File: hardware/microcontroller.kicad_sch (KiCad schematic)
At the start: 53 parts, among them J501 TC2050, J502 PRPC006SAAN-RC, J503 61300611121, J504 61300611121, J505 61300611121, J506 61300611121, J507 61300611121, J508 PRPC001DAAN-RC, J509 PRPC006SAAN-RC, SW501 430182050816, SW502 430182050816, U501 STM32L552CEU6, U502 AT25SF081B-MAHB-T, Y501 ECS-160-9-37-CKM-TR3, Y502 ABS05-32.768KHZ-9-T

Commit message: HW: Refactor the schematics
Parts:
- removed R504: 10 kΩ, perfect_footprints:R_0402_1005Metric, symbol Device:R
- added C516: 0.1 µF, perfect_footprints:C_0402_1005Metric, symbol Device:C
- added Q401: BSS806NH, Package_TO_SOT_SMD:SOT-23-3, symbol Transistor_FET:Q_NMOS_GSD
- added R403: 180 kΩ, perfect_footprints:R_0402_1005Metric, symbol Device:R
- added R404: 330 Ω, perfect_footprints:R_0402_1005Metric, symbol Device:R
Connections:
- net BAT_DETn: now also Q401.1 (G); no longer U501.11 (PA1)
- net EXT_FLASH_NCS: now also R511.2, U502.1 (~{CS}); no longer R511.1, U501.22 (PB11)
- net EXT_FLASH_SCK: now also R512.2, U502.6 (SCK); no longer R512.1, U501.21 (PB10)
- net GND: now also C516.2, Q401.2 (S)
- net V_3V3: now also R403.1
- net I2C_SCL renamed I2C.SCL
- net I2C_SDA renamed I2C.SDA
- net USB_DN renamed USB.DM
- net USB_DP renamed USB.DP
- net VDDA renamed V_DDA
- new net: C516.1, Q401.3 (D), R403.2, R404.1
- new net: R512.1, U501.21 (PB10)
- new net: R511.1, U501.22 (PB11)
- new net BAT_DET: R404.2, U501.11 (PA1)
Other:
- note removed: "Debug header"
- note removed: "Place R506 near the MCU pin. Place R502 near the connector."
- note removed: "Place the capacitor near the MCU pin."
- note removed: "Reset switch"
- note removed: "Use a common center pad."
- moved on the sheet: R503, R505, R511, R512

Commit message: Add EEPROM
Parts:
- removed C514, C516: 0.1 µF, perfect_footprints:C_0402_1005Metric, symbol Device:C
- removed R502, R506, R507, R511, R512, R513, R514, R515, R516: 22 Ω, perfect_footprints:R_0402_1005Metric, symbol Device:R
- removed R517, R518, R519, R520: 10 kΩ, perfect_footprints:R_0402_1005Metric, symbol Device:R
- removed U502: AT25SF081B-MAHB-T, Package_DFN_QFN:DFN-8-1EP_2x3mm_P0.5mm_EP0.61x2.2mm, symbol Renesas:AT25SF081-MAHB-X
- added C222: 1 µF, perfect_footprints:C_0201_0603Metric, symbol Device:C
- added R523, R524, R525, R526, R527: 27 Ω, perfect_footprints:R_0201_0603Metric, symbol Device:R
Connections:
- net DBG_UART_RX: now also J502.4 (Pin_4), R527.1; no longer U501.13 (PA3)
- net DBG_UART_TX: now also R526.2
- net GND: now also C222.2
- net MDM_TXD: now also R525.2
- net at J502.5 (Pin_5): now also R526.1
- net at Q401.3 (D), R403.2, R404.1: now also C222.1
- net at U501.42 (PB6): now also R525.1
- net at U501.21 (PB10): now also R524.1
- net at U501.22 (PB11): now also R523.1
- net EXT_FLASH_IO0 renamed FLASH_QSPI.IO0
- net EXT_FLASH_IO1 renamed FLASH_QSPI.IO1
- net EXT_FLASH_IO2 renamed FLASH_QSPI.IO2
- net EXT_FLASH_IO3 renamed FLASH_QSPI.IO3
- net HWID_1: no longer names the net of U501.14 (PA4)
- net HWID_2: no longer names the net of U501.15 (PA5)
- new net: R527.2, U501.13 (PA3)
- new net FLASH_QSPI.CSn: R523.2
- new net FLASH_QSPI.SCK: R524.2
- no-connect marks 9 -> 11
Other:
- note removed: "External flash"
- note removed: "Hardware ID map"
- note removed: "Use common center pads."
- moved on the sheet: R509

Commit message: Refine schematics
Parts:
- removed C501, C503, C504, C507, C508, C512, C515: 0.1 µF, perfect_footprints:C_0402_1005Metric, symbol Device:C
- removed C502, C513: 4.7 µF, Capacitor_SMD:C_0603_1608Metric, symbol Device:C
- removed C509: 0.01 μF, perfect_footprints:C_0402_1005Metric, symbol Device:C
- removed R403: 180 kΩ, perfect_footprints:R_0402_1005Metric, symbol Device:R
- removed R404, R503, R521: 330 Ω, perfect_footprints:R_0402_1005Metric, symbol Device:R
- removed R501, R505, R522: 10 kΩ, perfect_footprints:R_0402_1005Metric, symbol Device:R
- removed R508, R509: 4.7 kΩ, perfect_footprints:R_0402_1005Metric, symbol Device:R
- removed R510: 0 Ω, Resistor_SMD:R_0603_1608Metric, symbol Device:R
- added C18, C20, C21, C24, C25, C29, C31: 1 µF, perfect_footprints:C_0201_0603Metric, symbol Device:C
- added C19, C30: 4.7 µF, perfect_footprints:C_0402_1005Metric_HDI, symbol Device:C
- added C28: 0.1 µF, perfect_footprints:C_0201_0603Metric, symbol Device:C
- added R21: 180 kΩ, perfect_footprints:R_0201_0603Metric, symbol Device:R
- added R22, R24, R34: 330 Ω, perfect_footprints:R_0402_1005Metric, symbol Device:R
- added R23, R27, R35: 10 kΩ, perfect_footprints:R_0201_0603Metric, symbol Device:R
- added R31, R32: 2.2 kΩ, perfect_footprints:R_0201_0603Metric, symbol Device:R
- added R33: 0 Ω, Resistor_SMD:R_0603_1608Metric, symbol Device:R
- SW1: renamed from SW501; footprint Button_Switch_SMD:SW_SPST_PTS645 -> Button_Switch_SMD:SW_SPST_PTS645Sx43SMTR92
- SW2: renamed from SW502; footprint Button_Switch_SMD:SW_SPST_PTS645 -> Button_Switch_SMD:SW_SPST_PTS645Sx43SMTR92
- renumbered C222 to C17, C505 to C22, C506 to C23, C510 to C26, C511 to C27, J501 to J10, J502 to J11, J503 to J12, J504 to J13, J505 to J14, J506 to J15, J507 to J16, J508 to J17, J509 to J18, JP501 to JP1, Q401 to Q4, R526 to R25, R527 to R26, R523 to R28, R524 to R29, R525 to R30, U501 to U6, Y501 to Y1, Y502 to Y2
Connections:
- net BAT_DET: now also R22.2
- net BOOT0: now also R27.1
- net GND: now also C18.2, C19.2, C20.2, C21.2, C24.2, C25.2, C28.2, C29.2, C30.2, C31.2, R27.2
- net I2C.SCL: now also R31.2
- net I2C.SDA: now also R32.2
- net NRST: now also R24.2
- net USER_BUTTON: now also R34.1
- net V_3V3: now also C19.1, C20.1, C21.1, C24.1, C25.1, C30.1, R21.1, R23.1, R31.1, R32.1, R33.2, R35.1
- net V_DDA: now also C28.1, C29.1, R33.1
- net at SW1.1 (A): now also C18.1, R23.2, R24.1
- net at C17.1, Q4.3 (D): now also R21.2, R22.1
- net EEPROM_WCn: now reaches U6.14 (PA4)
- net at SW2.1 (A): now also C31.1, R34.2, R35.2
- no-connect marks 11 -> 10
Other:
- note added: "Notes"
- moved on the sheet: JP1, R26

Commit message: HW: Refine PDN
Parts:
- removed R33: 0 Ω, Resistor_SMD:R_0603_1608Metric, symbol Device:R
- added R88: 0 Ω, Resistor_SMD:R_0805_2012Metric, symbol Device:R
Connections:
- net V_3V3: now also R88.2
- net V_DDA: now also R88.1
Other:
- note added: "4.7 µF + 1 µF x VDD pin"
- note added: "Ferrite placeholder"
- note removed: "Placeholder for a ferrite if needed"
- moved on the sheet: C30

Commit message: HW: Switch MCU
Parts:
- removed C22, C23, C26, C27: 8 pF, perfect_footprints:C_0402_1005Metric, symbol Device:C
- removed R25, R28, R29: 27 Ω, perfect_footprints:R_0201_0603Metric, symbol Device:R
- removed R31, R32: 2.2 kΩ, perfect_footprints:R_0201_0603Metric, symbol Device:R
- removed U6: STM32L552CEU6, Package_DFN_QFN:QFN-48-1EP_7x7mm_P0.5mm_EP5.6x5.6mm, symbol STMicroelectronics:STM32L552CEU6
- added C58, C59, C60, C61: 8 pF, perfect_footprints:C_0201_0603Metric, symbol Device:C
- added R33, R89, R90, R91, R92: 27 Ω, perfect_footprints:R_0201_0603Metric, symbol Device:R
- added R93, R94: 2.2 kΩ, perfect_footprints:R_0201_0603Metric, symbol Device:R
- added U14: STM32L552CET6, Package_QFP:LQFP-48_7x7mm_P0.5mm, symbol MCU_ST_STM32L5:STM32L552CETx
- C19: value 4.7 µF -> 10 µF; Digi-Key Part Number 1276-6836-1-ND -> (none); MPN CL05A475MO5NUNC -> (none)
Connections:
- net BAT_DET: now also U14.11 (PA1)
- net BOOT0: now also U14.44 (PH3)
- net DBG_GPIO: now also U14.10 (PA0)
- net DBG_UART_RX: now also R26.2, U14.13 (PA3); no longer J11.4 (Pin_4), R26.1
- net DBG_UART_TX: now also J11.5 (Pin_5), R33.2
- net DEBUG_SWCLK: now also U14.37 (PA14)
- net DEBUG_SWDIO: now also U14.34 (PA13)
- net DEBUG_SWO: now also U14.39 (PB3)
- net EEPROM_WCn: now also U14.14 (PA4)
- net FLASH_QSPI.CSn: now also R89.1
- net FLASH_QSPI.IO0: now also U14.19 (PB1)
- net FLASH_QSPI.IO1: now also U14.18 (PB0)
- net FLASH_QSPI.IO2: now also U14.17 (PA7)
- net FLASH_QSPI.IO3: now also U14.16 (PA6)
- net FLASH_QSPI.SCK: now also R90.1
- net GND: now also C58.2, C59.2, C60.2, C61.2, U14.23 (VSS), U14.35 (VSS), U14.47 (VSS), U14.8 (VSSA)
- net GPIO_PA15: now also U14.38 (PA15)
- net GPIO_PA8: now also U14.29 (PA8)
- net GPIO_PA9: now also U14.30 (PA9)
- net GPIO_PB12: now also U14.25 (PB12)
- net GPIO_PB15: now also U14.28 (PB15)
- net GPIO_PB4: now also U14.40 (PB4)
- net GPIO_PB5: now also U14.41 (PB5)
- net GPIO_PB8: now also U14.45 (PB8)
- net GPIO_PB9: now also U14.46 (PB9)
- net I2C.SCL: now also R91.1, R94.2
- net I2C.SDA: now also R92.1, R93.2
- net IO_EXP_INT: now also U14.2 (PC13)
- net MDM_RXD: now also U14.43 (PB7)
- net MDM_TXD: now also R30.1; no longer R30.2
- net NRST: now also U14.7 (NRST)
- net USB.DM: now also U14.31 (PA10)
- net USB.DP: now also U14.32 (PA11)
- net V_3V3: now also R93.1, R94.1, U14.1 (VBAT), U14.24 (VDD), U14.36 (VDD), U14.48 (VDD)
- net V_DDA: now also U14.9 (VDDA)
- net OSC16M_IN renamed HSE_IN
- net HSE_IN: now also C58.1, U14.5 (PH0)
- net OSC16M_OUT renamed HSE_OUT
- net HSE_OUT: now also C59.1, U14.6 (PH1)
- net OSC32K_IN renamed LSE_IN
- net LSE_IN: now also C60.1, U14.3 (PC14)
- net OSC32K_OUT renamed LSE_OUT
- net LSE_OUT: now also C61.1, U14.4 (PC15)
- new net: J11.4 (Pin_4), R26.1
- new net: R89.2, U14.22 (PB11)
- new net: R33.1, U14.12 (PA2)
- new net: R90.2, U14.21 (PB10)
- new net: R91.2, U14.26 (PB13)
- new net: R92.2, U14.27 (PB14)
- new net: R30.2, U14.42 (PB6)
- new net GPIO_PA12: U14.33 (PA12)
- new net GPIO_PA5: U14.15 (PA5)
- new net GPIO_PB2: U14.20 (PB2)
- no-connect marks 10 -> 8
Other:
- note added: "Outputs"
- moved on the sheet: C17, C18, C19, C20, C21, C24, C25, C28, C29, C30, C31, J10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

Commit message: HW: Refine schematics
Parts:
- removed J17: PRPC001DAAN-RC, Connector_PinHeader_2.54mm:PinHeader_1x02_P2.54mm_Vertical, symbol Connector_Generic:Conn_01x02
- removed R89, R90: 27 Ω, perfect_footprints:R_0201_0603Metric, symbol Device:R
- added R28: 10 kΩ, perfect_footprints:R_0201_0603Metric, symbol Device:R
- added R95, R96, R97: 27 Ω, perfect_footprints:R_0201_0603Metric, symbol Device:R
- J11: now fitted; now in the parts list
- R34: Digi-Key Part Number 732-560112110231CT-ND -> (none); MPN 560112110231 -> (none)
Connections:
- net GPIO_PA10 is gone; now on net GPIO_PA5: J13.1 (Pin_1)
- net GPIO_PA12 is gone; now on net USB.DP: U14.33 (PA12)
- net BAT_DETn: now also R22.2, U14.42 (PB6); no longer Q4.1 (G)
- net BOOT0: now also R28.2
- net DBG_UART_RX: no longer U14.13 (PA3)
- net DBG_UART_TX: no longer R33.2
- net EEPROM_WCn: now also U14.43 (PB7); no longer U14.14 (PA4)
- net FLASH_QSPI.CSn: now also R96.2
- net FLASH_QSPI.SCK: now also R97.2
- net GND: no longer J15.3 (Pin_3)
- net GPIO_PA15: now also J14.5 (Pin_5), JP1.1 (A); no longer J13.3 (Pin_3)
- net GPIO_PA8: now also J14.3 (Pin_3); no longer J12.3 (Pin_3)
- net GPIO_PB12: now also J13.5 (Pin_5); no longer J15.1 (Pin_1)
- net GPIO_PB15: now also J14.1 (Pin_1); no longer J12.5 (Pin_5)
- net GPIO_PB2: now also J13.3 (Pin_3)
- net GPIO_PB4: now also J15.1 (Pin_1); no longer J13.5 (Pin_5)
- net GPIO_PB5: now also J15.3 (Pin_3); no longer J14.1 (Pin_1)
- net MDM_CTS: now also U14.26 (PB13)
- net MDM_RTS: now also R95.1
- net MDM_RXD: now also U14.22 (PB11); no longer U14.43 (PB7)
- net USB.DM: now also U14.32 (PA11); no longer U14.31 (PA10)
- net USB.DP: no longer U14.32 (PA11)
- net V_3V3: now also R28.1
- net at R33.1: now also U14.30 (PA9); no longer U14.12 (PA2)
- net at U14.21 (PB10): now also R30.2
- net at R91.2: now also U14.45 (PB8); no longer U14.26 (PB13)
- net at U14.27 (PB14): now also R95.2; no longer R92.2
- net BAT_DET renamed GPIO_PA1
- net GPIO_PA1: now also J12.3 (Pin_3); no longer R22.2
- net DBG_GPIO renamed GPIO_PA0
- net GPIO_PA0: now also J12.1 (Pin_1)
- removed net GPIO_PA9: J12.1 (Pin_1), JP1.1 (A), U14.30 (PA9)
- removed net GPIO_PB8: J14.3 (Pin_3), U14.45 (PB8)
- net GPIO_PB9: no longer names the net of U14.46 (PB9)
- net GPIO_PB9: now also R92.2; no longer J14.5 (Pin_5)
- net IO_EXP_INT renamed IO_EXP_INTn
- net NRST renamed RESETn
- new net: R96.1, U14.14 (PA4)
- new net: R97.1, U14.13 (PA3)
- new net DEBUG_RXD: U14.31 (PA10)
- new net DEBUG_TXD: R33.2
- new net GPIO_PA2: J12.5 (Pin_5), U14.12 (PA2)
- new net ST: Q4.1 (G)
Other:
- note added: "Inputs"
- note added: "MCU"
- moved on the sheet: C17, C18, C31, C58, C59, C60, C61, J10, J12, J13, J14, J15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

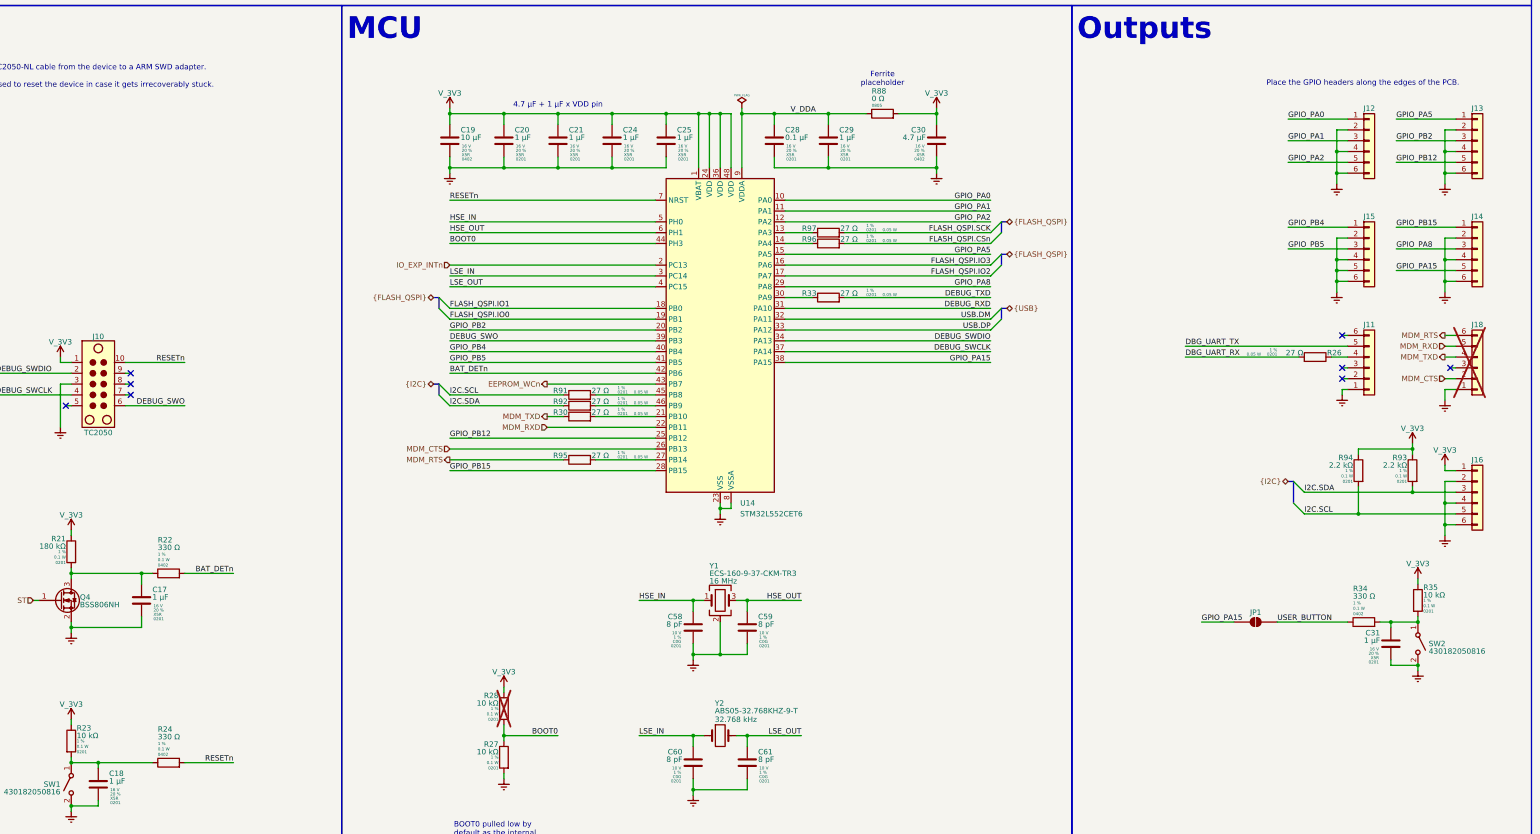
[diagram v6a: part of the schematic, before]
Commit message: HW: Redo MDM UART
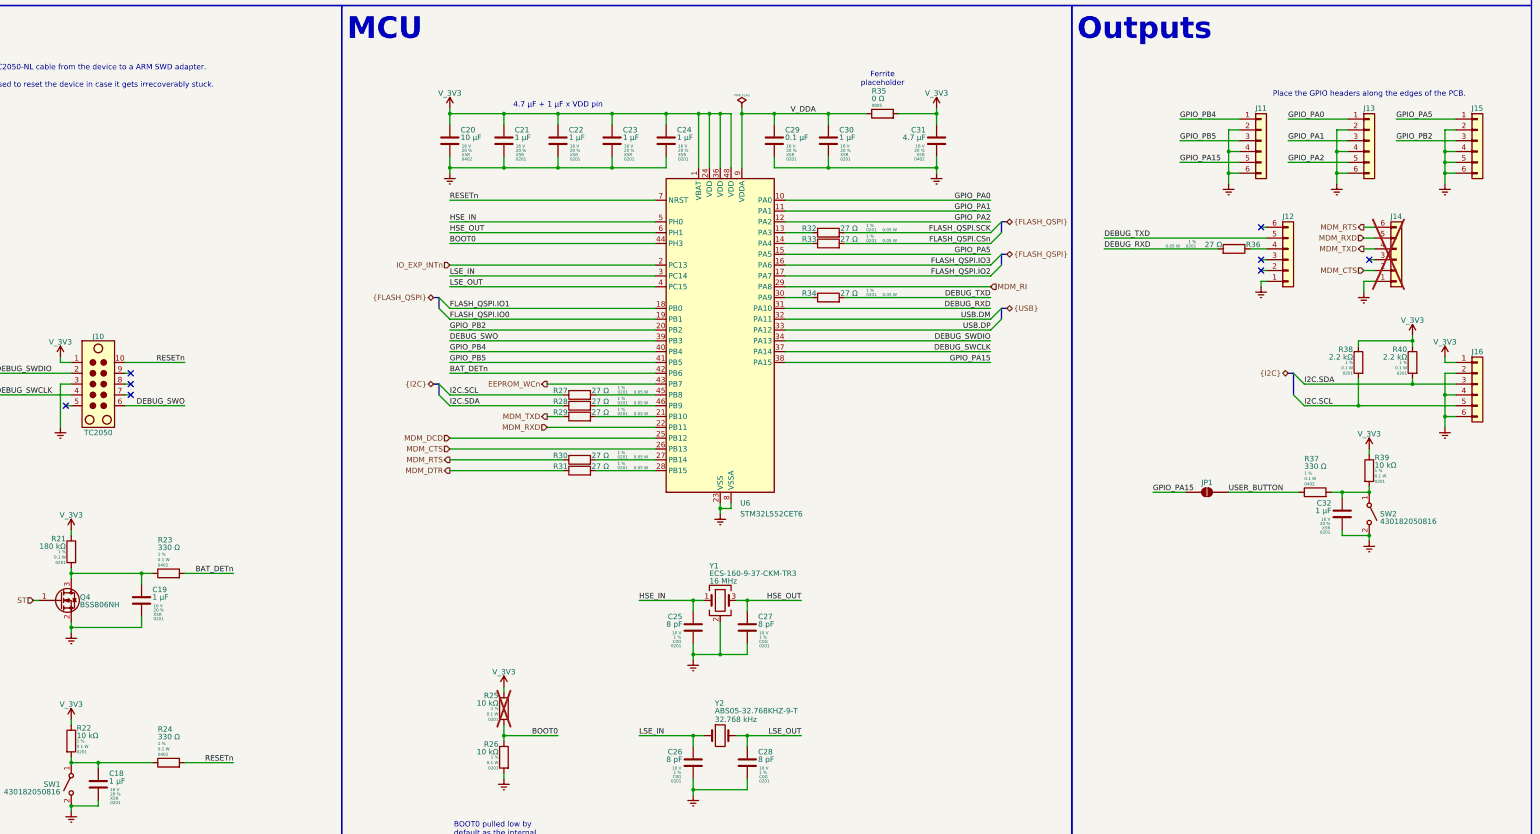
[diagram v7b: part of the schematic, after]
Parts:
- removed J14: 61300611121, Connector_PinHeader_2.54mm:PinHeader_1x06_P2.54mm_Vertical, symbol Connector_Generic:Conn_01x06
- added R31: 27 Ω, perfect_footprints:R_0201_0603Metric, symbol Device:R
- renumbered C17 to C19, C19 to C20, C20 to C21, C21 to C22, C24 to C23, C25 to C24, C58 to C25, C60 to C26, C59 to C27, C61 to C28, C28 to C29, C29 to C30, C30 to C31, C31 to C32, J15 to J11, J11 to J12, J12 to J13, J18 to J14, J13 to J15, R23 to R22, R22 to R23, R28 to R25, R27 to R26, R91 to R27, R92 to R28, R30 to R29, R95 to R30, R97 to R32, R96 to R33, R33 to R34, R88 to R35, R26 to R36, R34 to R37, R94 to R38, R35 to R39, R93 to R40, U14 to U6
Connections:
- net DBG_UART_RX is gone; now on net DEBUG_RXD: R36.2
- net DBG_UART_TX is gone; now on net DEBUG_TXD: J12.5 (Pin_5)
- net GND: now also J15.5 (Pin_5); no longer J11.5 (Pin_5)
- net GPIO_PA15: now also J11.5 (Pin_5)
- net GPIO_PA8 renamed MDM_RI
- net GPIO_PB12 renamed MDM_DCD
- net MDM_DCD: no longer J15.5 (Pin_5)
- net GPIO_PB15: no longer names the net of U6.28 (PB15)
- net GPIO_PB15: now also R31.2
- new net MDM_DTR: R31.1
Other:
- moved on the sheet: C32, J11, J12, J14, J16, JP1, R36, R37, R38, R39, R40, SW2

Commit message: HW: BAT_DETn -> USB_DET
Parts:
- renumbered C18 to C301, C19 to C302, C20 to C303, C21 to C304, C22 to C305, C23 to C306, C24 to C307, C25 to C308, C26 to C309, C27 to C310, C28 to C311, C29 to C312, C30 to C313, C31 to C314, C32 to C315, J10 to J301, J11 to J302, J12 to J303, J13 to J304, J14 to J305, J15 to J306, J16 to J307, JP1 to JP301, Q4 to Q301, R21 to R301, R22 to R302, R23 to R303, R24 to R304, R25 to R305, R26 to R306, R27 to R307, R28 to R308, R29 to R309, R30 to R310, R31 to R311, R32 to R312, R33 to R313, R34 to R314, R35 to R315, R36 to R316, R37 to R317, R38 to R318, R39 to R319, R40 to R320, SW1 to SW301, SW2 to SW302, U6 to U301, Y1 to Y301, Y2 to Y302
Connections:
- net BAT_DETn renamed USB_DET
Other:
- moved on the sheet: C301, C302, J301, Q301, R301, R302, R303, R304, SW301
